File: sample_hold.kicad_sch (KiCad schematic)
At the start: 38 parts, among them U31 OPA828DGN, U32 TCA0372, U33 OPA2197xDGK, U35 MAX4649EKA+

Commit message: More work in progres
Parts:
- added C206: 1n, Capacitor_SMD:C_0603_1608Metric, symbol Device:C
- added D206: 1N4148WT, Diode_SMD:D_SOD-523, symbol Diode:1N4148WT
- added JP21: SolderJumper_2_Open, symbol Jumper:SolderJumper_2_Open
- C202: renamed from C?; value 10n -> 33n
- R203, R204, R205, R206: renamed from R?; value 330 -> 1k
- R207: renamed from R?; value 100 -> 1k
- RN21: renamed from RN?; now fitted
- U22: renamed from U33; value OPA2197xDGK -> OPA2197xD; footprint Package_SO:VSSOP-8_3x3mm_P0.65mm -> Package_SO:SOIC-8_3.9x4.9mm_P1.27mm; symbol Amplifier_Operational:OPA2197xDGK -> Amplifier_Operational:OPA2197xD
- gave numbers to parts that had none: 25
- renumbered U32 to U19, U31 to U21, U35 to U23
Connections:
- net Drive: now also C202.2
- net SampleGnd: now also JP21.1 (A); no longer Q206.2 (S)
- net at Q202.3 (D): now also D206.2 (A); no longer D205.2 (A)
- net at R201.1, U22.2 (-): now also R202.2, C206.1; no longer C202.1, R213.2
- net at R202.1: now also C202.1, R213.2; no longer U19.9 (+)
- net at R212.2, R213.1: now also U22.7; no longer U22.1
- net at R211.2, R212.1: now also U22.6 (-); no longer U22.2 (-)
- net AGND renamed GND
- net GND: now also U22.5 (+); no longer U22.3 (+)
- net PGND renamed GNDPWR
- new net: C206.2, U19.9 (+), U22.1
- new net: D205.2 (A), D206.1 (K)
- new net: JP21.2 (B), Q206.2 (S)
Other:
- note added: "TODO: Diode current."
- note added: "TODO: Jellybean"
- moved on the sheet: C202, Q202, Q203, Q204, Q205, Q206, Q207, R202, R208, R211, R212, R213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

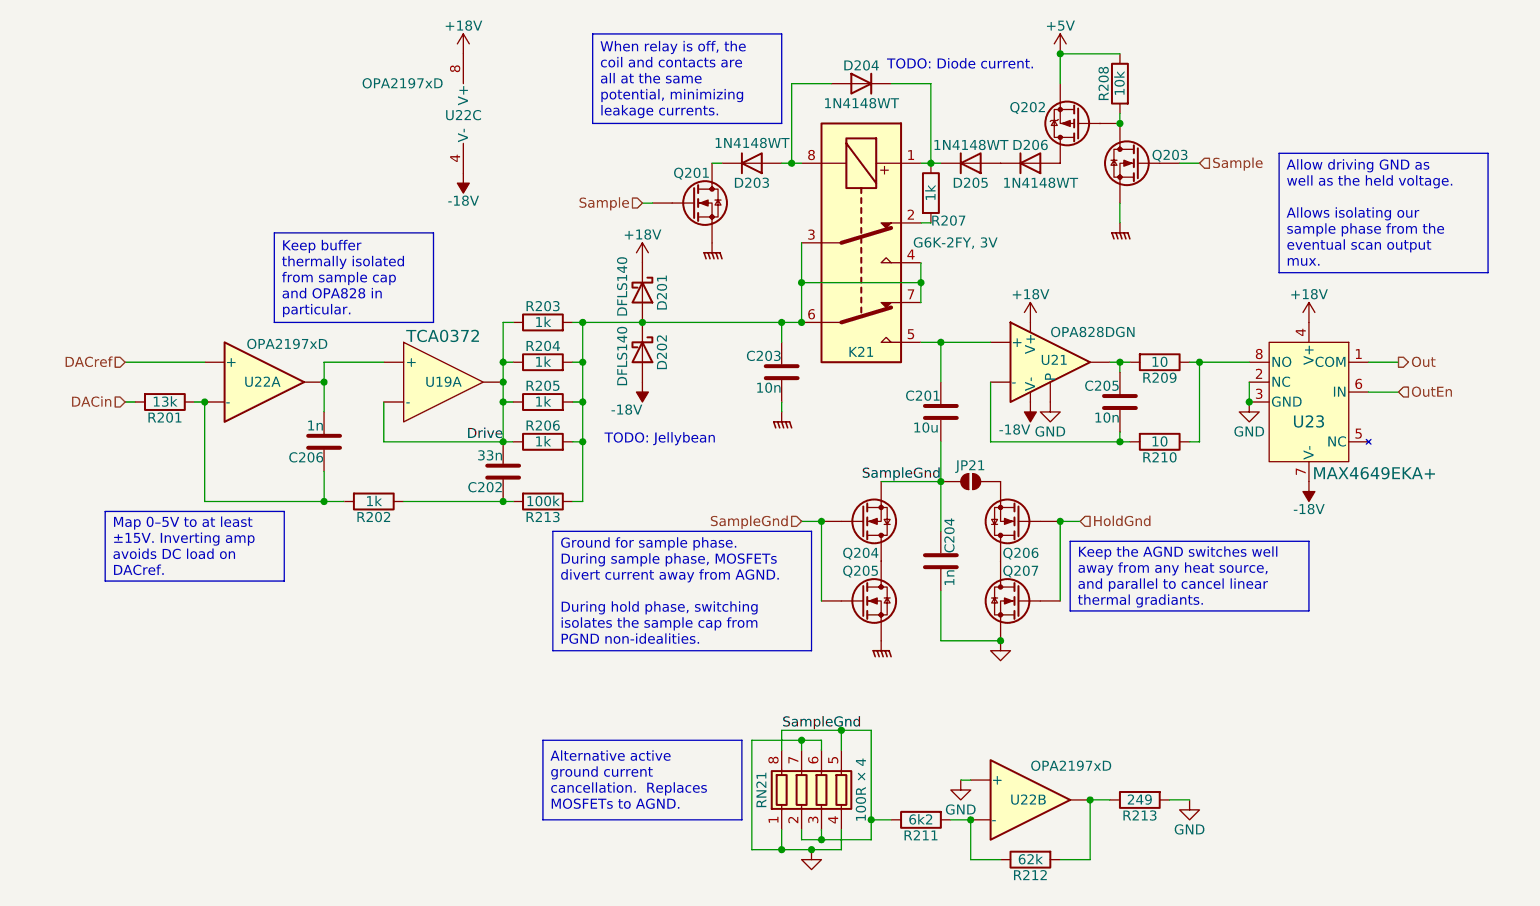
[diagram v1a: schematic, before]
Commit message: Analog side is more or less complete.
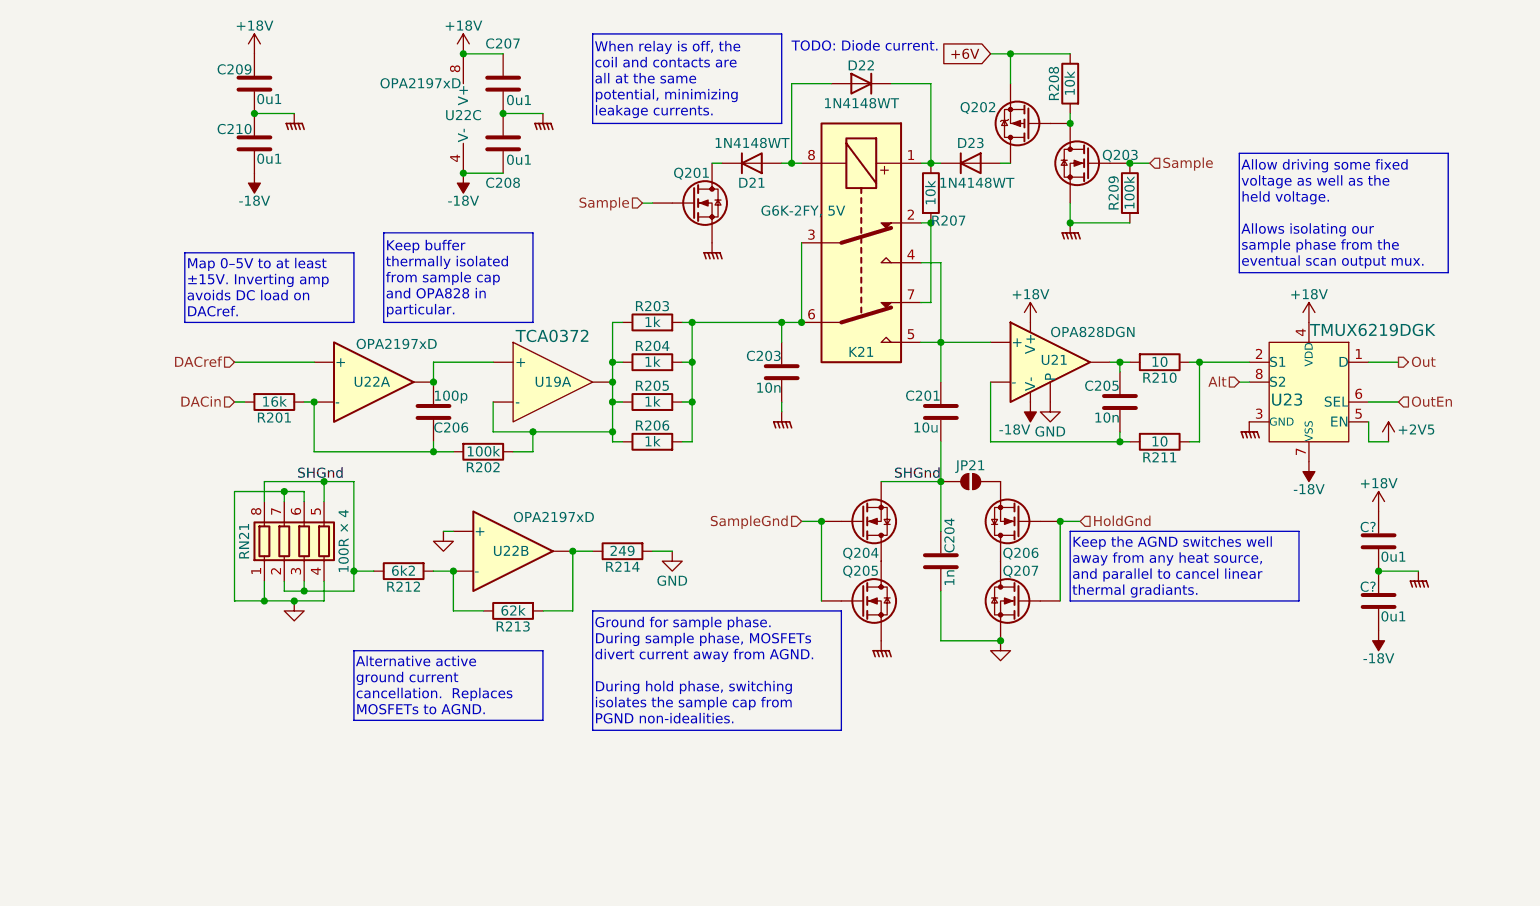
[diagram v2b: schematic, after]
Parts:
- removed C202: 33n, Capacitor_SMD:C_0603_1608Metric, symbol Device:C
- removed D201, D202: DFLS140, Diode_SMD:D_SMA, symbol Diode:SS34
- removed D206: 1N4148WT, Diode_SMD:D_SOD-523, symbol Diode:1N4148WT
- removed R213: 100k, Resistor_SMD:R_0603_1608Metric, symbol Device:R
- added C207, C208, C209, C210, C? (x2): 0u1, symbol Device:C
- added R209: 100k, symbol Device:R
- C206: value 1n -> 100p
- K21: value G6K-2FY, 3V -> G6K-2FY, 5V
- R201: value 13k -> 16k
- R202: value 1k -> 100k
- R207: value 1k -> 10k
- U23: value MAX4649EKA+ -> TMUX6219DGK; footprint 21-0078H_MXM -> SOIC8_DGK_TEX; symbol Parts:MAX4649EKA+ -> Parts:TMUX6219DGK
- renumbered D203 to D21, D204 to D22, D205 to D23, R209 to R210, R210 to R211, R211 to R212, R212 to R213, R213 to R214
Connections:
- net Drive is gone; now on an unnamed net: R203.1, R204.1, R205.1, R206.1, U19.10 (-), U19.16
- net +18V: now also C207.1, C209.1, C?.1
- net -18V: now also C208.2, C210.2, C?.2
- net GND: no longer U23.2 (NC), U23.3 (GND)
- net GNDPWR: now also U23.3 (GND), C207.2, C208.1, C209.2, C210.1, C?.1, C?.2, R209.2
- net Sample: now also R209.1
- net SampleGnd: no longer C201.2, C204.1, JP21.1 (A), Q204.2 (S), R212.1, RN21.2 (R2.1), RN21.3 (R3.1), RN21.5 (R4.2), RN21.8 (R1.2)
- net at Q202.3 (D): now also D23.2 (A)
- net +2V5: now reaches U23.5 (EN)
- net at R210.1, R211.1: now also U23.2 (S1); no longer U23.8 (NO)
- net at K21.2, R207.2: now also K21.7
- net at C203.2, K21.3, K21.6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: no longer K21.4, K21.7
- net at C201.1, K21.5, U21.3 (+): now also K21.4
- net +5V renamed +6V
- new net Alt: U23.8 (S2)
- new net SHGnd: C201.2, C204.1, JP21.1 (A), Q204.2 (S), R212.1, RN21.2 (R2.1), RN21.3 (R3.1), RN21.5 (R4.2), RN21.8 (R1.2)
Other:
- note removed: "TODO: Jellybean"
- moved on the sheet: C206, Q202, Q203, R201, R202, R203, R204, R205, R206, R208, R212, R213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

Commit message: Schematic complete, maybe
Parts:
- added C212: 10u, Capacitor_SMD:C_0603_1608Metric, symbol Device:C
- added L21: 600, Inductor_SMD:L_0603_1608Metric, symbol Parts:L_Ferrite_Power
- C201: footprint (none) -> Big, 27.5mm pitch
- C202: renamed from C206; LCSC (none) -> C14858
- C203, C205: footprint (none) -> Capacitor_SMD:C_0603_1608Metric; LCSC (none) -> C307500
- C204: footprint (none) -> Capacitor_SMD:C_0603_1608Metric; now left out of the parts list
- C206: renamed from C209; footprint (none) -> Capacitor_SMD:C_0402_1005Metric; LCSC (none) -> C307331
- C207: renamed from C210; footprint (none) -> Capacitor_SMD:C_0402_1005Metric; LCSC (none) -> C307331
- C208: renamed from C207; footprint (none) -> Capacitor_SMD:C_0402_1005Metric; LCSC (none) -> C307331
- C209: renamed from C208; footprint (none) -> Capacitor_SMD:C_0402_1005Metric; LCSC (none) -> C307331
- C210, C211: renamed from C?; footprint (none) -> Capacitor_SMD:C_0402_1005Metric; LCSC (none) -> C307331
- U19: now left out of the parts list
- U21: LCSC (none) -> C20345611
- U22: LCSC (none) -> C139363; now left out of the parts list
- U23: LCSC (none) -> C2876423
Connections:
- net +6V: now also L21.1; no longer Q202.2 (S), R208.1
- net GNDPWR: now also C212.2
- net at C203.2, K21.3, K21.6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: now also K21.4
- net at C201.1, K21.5, U21.3 (+): no longer K21.4
- new net: C212.1, L21.2, Q202.2 (S), R208.1

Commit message: Part selection
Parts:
- removed D21, D23: 1N4148WT, Diode_SMD:D_SOD-523, symbol Diode:1N4148WT
- added D21, D23: SM4007PL, Parts:D_SOD-123FL, symbol Parts:SM4007PL
- D22: value 1N4148WT -> 1N5819WS; footprint Diode_SMD:D_SOD-523 -> Diode_SMD:D_SOD-323; symbol Diode:1N4148WT -> Parts:1N5819WS; LCSC (none) -> C191023
- K21: now left out of the parts list
- Q201, Q203, Q204, Q205, Q206, Q207: LCSC (none) -> C20917
- Q202: LCSC (none) -> C15127
- R201: LCSC (none) -> C22818
- R202, R209: footprint (none) -> Resistor_SMD:R_0402_1005Metric; LCSC (none) -> C25741
- R203, R204, R205, R206: footprint Resistor_SMD:R_1206_3216Metric -> Resistor_SMD:R_0805_2012Metric; LCSC (none) -> C17513
- R207, R208: footprint (none) -> Resistor_SMD:R_0402_1005Metric; LCSC (none) -> C25744
- R210, R211: footprint (none) -> Resistor_SMD:R_0402_1005Metric; LCSC (none) -> C25077
- R212: footprint (none) -> Resistor_SMD:R_0603_1608Metric; LCSC (none) -> C4260
- R213: footprint (none) -> Resistor_SMD:R_0603_1608Metric; LCSC (none) -> C23221
- R214: footprint (none) -> Resistor_SMD:R_0603_1608Metric; now left out of the parts list
- RN21: footprint (none) -> Resistor_SMD:R_Array_Convex_4x0603
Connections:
- net at Q202.3 (D): now also D23.2 (A)
- net at D22.1 (K), K21.1, R207.1: now also D23.1 (K)
- net at D22.2 (A), K21.8: now also D21.2 (A)
- net at Q201.3 (D): now also D21.1 (K)
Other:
- note removed: "TODO: Diode current."

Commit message: ERC passes.
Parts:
- C201: footprint Big, 27.5mm pitch -> Capacitor_THT:C_Rect_L31.5mm_W15.0mm_P27.50mm_MKS4; now left out of the parts list
- C202: value 100p -> 0n1
- D22: value 1N5819WS -> SM4007PL; footprint Diode_SMD:D_SOD-323 -> Parts:D_SOD-123FL; symbol Parts:1N5819WS -> Parts:SM4007PL
- RN21: now left out of the parts list
- U22: value OPA2197xD -> OPA2197D
- U23: footprint SOIC8_DGK_TEX -> Package_SO:VSSOP-8_3x3mm_P0.65mm
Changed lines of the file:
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@@
 	)
 	(symbol
+		(lib_name "AO3400A_2")
 		(lib_id "Transistor_FET:AO3400A")
 		(at 156.21 97.79 0)
@@
 	)
 	(symbol
+		(lib_name "OPA2197xD_1")
 		(lib_id "Amplifier_Operational:OPA2197xD")
 		(at 93.98 69.85 0)
@@
 			)
 		)
-		(property "Value" "OPA2197xD"
-			(at 91.694 65.024 0)
+		(property "Value" "OPA2197D"
+			(at 96.774 65.532 0)
 			(effects
 				(font
 					(size 1.27 1.27)
 				)
-				(justify left)
 			)
 		)
@@
 			)
 		)
-		(property "Footprint" "SOIC8_DGK_TEX"
+		(property "Footprint" "Package_SO:VSSOP-8_3x3mm_P0.65mm"
 			(at 213.36 71.12 0)
 			(effects
@@
 	)
 	(symbol
-		(lib_id "Parts:1N5819WS")
+		(lib_id "Parts:SM4007PL")
 		(at 156.21 31.75 0)
 		(mirror y)
@@
 			)
 		)
-		(property "Value" "1N5819WS"
+		(property "Value" "SM4007PL"
 			(at 156.21 34.29 0)
 			(effects
@@
 			)
 		)
-		(property "Footprint" "Diode_SMD:D_SOD-323"
+		(property "Footprint" "Parts:D_SOD-123FL"
 			(at 156.21 36.195 0)
 			(effects
@@
 			)
 		)
-		(property "Description" "40V 600mV@1A 1A SOD-323 Schottky Barrier Diodes, SOD-323"
+		(property "Description" "1000V, 1A, General Purpose Rectifier Diode, SMA(DO-214AC)"
 			(at 156.21 31.75 0)
 			(effects
@@
 			(project "lincal"
 				(path "/b054cef4-39e3-49d8-aff0-7ba5a206c187/6f91b1d1-06a0-428d-b546-bc9bd4fa19a0"
-					(reference "D?")
+					(reference "D28")
 					(unit 1)
 				)
@@
 			)
 		)
-		(property "Value" "100p"
+		(property "Value" "0n1"
 			(at 101.6 71.628 0)
 			(effects
@@
 	)
 	(symbol
+		(lib_name "AO3400A_3")
 		(lib_id "Transistor_FET:AO3400A")
 		(at 185.42 41.91 0)
@@
 	)
 	(symbol
+		(lib_name "AO3400A_1")
 		(lib_id "Transistor_FET:AO3400A")
 		(at 156.21 87.63 0)
@@
 	)
 	(symbol
+		(lib_name "AO3400A_5")
 		(lib_id "Transistor_FET:AO3400A")
 		(at 176.53 87.63 180)
@@
 		(unit 1)
 		(exclude_from_sim no)
-		(in_bom yes)
+		(in_bom no)
 		(on_board yes)
 		(dnp no)
@@
 		)
 		(property "Value" "10u"
-			(at 166.116 75.692 0)
+			(at 166.37 75.692 0)
 			(effects
 				(font
@@
 			)
 		)
-		(property "Footprint" "Big, 27.5mm pitch"
+		(property "Footprint" "Capacitor_THT:C_Rect_L31.5mm_W15.0mm_P27.50mm_MKS4"
 			(at 165.4048 77.47 0)
 			(effects
@@
 			)
 		)
-		(property "Value" "OPA2197xD"
+		(property "Value" "OPA2197D"
 			(at 105.156 31.75 0)
 			(effects
@@
 			(project ""
 				(path "/b054cef4-39e3-49d8-aff0-7ba5a206c187/6f91b1d1-06a0-428d-b546-bc9bd4fa19a0"
-					(reference "D?")
+					(reference "D27")
 					(unit 1)
 				)
@@
 		(unit 1)
 		(exclude_from_sim no)
-		(in_bom yes)
+		(in_bom no)
 		(on_board yes)
 		(dnp no)
@@
 	)
 	(symbol
+		(lib_name "AO3400A_4")
 		(lib_id "Transistor_FET:AO3400A")
 		(at 134.62 46.99 0)
@@
 	)
 	(symbol
+		(lib_name "OPA2197xD_2")
 		(lib_id "Amplifier_Operational:OPA2197xD")
 		(at 111.76 91.44 0)
@@
 			)
 		)
-		(property "Value" "OPA2197xD"
-			(at 111.76 87.122 0)
+		(property "Value" "OPA2197D"
+			(at 115.316 87.376 0)
 			(effects
 				(font
 					(size 1.27 1.27)
 				)
-				(justify left)
 			)
 		)

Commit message: Everything assigned except for wierd shit.
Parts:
- C204: value 1n -> 100p; footprint Capacitor_SMD:C_0603_1608Metric -> Capacitor_SMD:C_0402_1005Metric; LCSC (none) -> C1546; now in the parts list
- D22: LCSC C191023 -> C64898
- JP21: footprint (none) -> Parts:ThermJump
- R211: value 10 -> 100; LCSC C25077 -> C25076
- R212: value 6k2 -> 1k; footprint Resistor_SMD:R_0603_1608Metric -> Resistor_SMD:R_0402_1005Metric; LCSC C4260 -> C11702
- R213: value 62k -> 8k2; LCSC C23221 -> C25981
- R214: value 249 -> 200; footprint Resistor_SMD:R_0603_1608Metric -> Resistor_SMD:R_0402_1005Metric; LCSC (none) -> C25087; now in the parts list
- U23: value TMUX6219DGK -> DG419D; footprint Package_SO:VSSOP-8_3x3mm_P0.65mm -> Package_SO:SOIC-8_3.9x4.9mm_P1.27mm; symbol Parts:TMUX6219DGK -> Parts:DG419; now left out of the parts list
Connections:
- net SHGnd: no longer C204.1
- net at JP21.2 (B), Q206.2 (S): now also C204.1
- net +2V5 renamed +3V3A
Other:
- moved on the sheet: C204, Q204, Q205, Q206, Q207

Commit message: Layout underway
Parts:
- JP21: footprint Parts:ThermJump -> Parts:ThermJump_1
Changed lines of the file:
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@@
 			)
 		)
-		(property "Footprint" "Parts:ThermJump"
+		(property "Footprint" "Parts:ThermJump_1"
 			(at 170.18 82.55 0)
 			(effects
@@
 		)
 		(property "Value" "OPA2197D"
-			(at 105.156 31.75 0)
-			(effects
-				(font
-					(size 1.27 1.27)
-				)
-				(justify left)
-			)
-		)
+			(at 101.6 35.56 90)
+			(effects
+				(font
+					(size 1.27 1.27)
+				)
+			)
+		)
